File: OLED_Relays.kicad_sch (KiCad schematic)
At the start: 0 parts

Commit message: OLED, Relay and Bar graph added
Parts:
- added BAR1: HDSP-4830_2, Display:HDSP-4830, symbol LED:HDSP-4830_2
- added D17, D18: 1N4148, Diode_THT:D_DO-35_SOD27_P7.62mm_Horizontal, symbol Lattice_DVK:1N4148
- added J3, J4: Relay, TerminalBlock_Phoenix:TerminalBlock_Phoenix_MKDS-1,5-3-5.08_1x03_P5.08mm_Horizontal, symbol Lattice_DVK:Screw_Terminal_01x03
- added J5: RELAY, symbol Connector:Conn_01x04_Pin
- added J6: OLED, symbol Connector:Conn_01x04_Pin
- added K1: SANYOU_SRD_Form_C, LOGSUN:LGS-KC-FRS1B, symbol Lattice_DVK:SANYOU_SRD_Form_C_1
- added K2: SANYOU_SRD_Form_C, LOGSUN:LGS-KC-FRS1B, symbol Lattice_DVK:SANYOU_SRD_Form_C
- added Q4, Q5: BC847, Package_TO_SOT_SMD:SOT-23, symbol Lattice_DVK:BC847
- added Q6, Q7: BC858, Package_TO_SOT_SMD:SOT-23, symbol Lattice_DVK:BC858
- added R28, R29, R32, R33: 4.7K, Resistor_SMD:R_1206_3216Metric_Pad1.30x1.75mm_HandSolder, symbol Lattice_DVK:R_Small
- added R30, R31, R34, R35: 10K, Resistor_SMD:R_1206_3216Metric_Pad1.30x1.75mm_HandSolder, symbol Lattice_DVK:R_Small
- added RN1, RN2, RN3: R_Pack04, symbol Device:R_Pack04
- added SV1: Bar_Graph-I, LOGSUN:LGS-KC-ML10_INTERFACE, symbol LOGSUN:LGS-KC-ML10_INTERFACE
- added SV2: Bar_Graph-II, LOGSUN:LGS-KC-ML10_INTERFACE, symbol LOGSUN:LGS-KC-ML10_INTERFACE
- added U5: 0.96" OLED(I2C), nitin:OLED I2C, symbol NITIN:OLED_I2C
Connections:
- new net: Q4.1 (B), R28.2, R30.1
- new net: Q7.1 (B), R33.1, R35.2
- new net: D18.1 (K), K2.3, Q7.3 (C)
- new net: D17.1 (K), K1.3, Q6.3 (C)
- new net: Q6.1 (B), R32.1, R34.2
- new net: Q4.3 (C), R32.2
- new net: Q5.3 (C), R33.2
- new net: Q5.1 (B), R29.2, R31.1
- new net BAR 1: BAR1.1 (A), RN1.8 (R1.2)
- new net BAR 10: BAR1.10 (A), RN3.7 (R2.2)
- new net BAR 2: BAR1.2 (A), RN1.7 (R2.2)
- new net BAR 3: BAR1.3 (A), RN1.6 (R3.2)
- new net BAR 4: BAR1.4 (A), RN1.5 (R4.2)
- new net BAR 5: BAR1.5 (A), RN2.8 (R1.2)
- new net BAR 6: BAR1.6 (A), RN2.7 (R2.2)
- new net BAR 7: BAR1.7 (A), RN2.6 (R3.2)
- new net BAR 8: BAR1.8 (A), RN2.5 (R4.2)
- new net BAR 9: BAR1.9 (A), RN3.8 (R1.2)
- new net COM_1: J3.2 (Pin_2), K1.5, K1.6
- new net COM_2: J4.2 (Pin_2), K2.5, K2.6
- new net GND_{Bar}: BAR1.11 (K), BAR1.12 (K), BAR1.13 (K), BAR1.14 (K), BAR1.15 (K), BAR1.16 (K), BAR1.17 (K), BAR1.18 (K), BAR1.19 (K), BAR1.20 (K), SV1.2, SV2.2
- new net GND_{OLED}: J6.4 (Pin_4), U5.2 (GND)
- new net GND_{RB}: D17.2 (A), D18.2 (A), J5.4 (Pin_4), K1.4, K2.4, Q4.2 (E), Q5.2 (E), R30.2, R31.2
- new net LD 1: SV1.3
- new net LD 2: SV1.4
- new net LD 3: SV1.5
- new net LD 4: SV1.6
- new net LD 5: SV1.7
- new net LD 6: SV1.8
- new net LD 7: SV1.9
- new net LD 8: SV1.10
- new net NC_1: J3.3 (Pin_3), K1.2
- new net NC_2: J4.3 (Pin_3), K2.2
- new net NO_1: J3.1 (Pin_1), K1.1
- new net NO_2: J4.1 (Pin_1), K2.1
- new net Relay_1: J5.2 (Pin_2), R28.1
- new net Relay_2: J5.3 (Pin_3), R29.1
- new net SCL: J6.2 (Pin_2), U5.3 (SCL)
- new net SDA: J6.3 (Pin_3), U5.4 (SDA)
- new net VCC_{OLED}: J6.1 (Pin_1), U5.1 (VCC)
- new net VCC_{RB}: J5.1 (Pin_1), Q6.2 (E), Q7.2 (E), R34.1, R35.1
- no-connect marks 0 -> 12
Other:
- note added: "0.96" OLED"
- note added: "Connectors"
- note added: "LED-Bar-Graph"
- note added: "Relay_{1}"
- note added: "Relay_{2}"

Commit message: Schematic Completed, Footprints Assigned
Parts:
- J3: value Relay -> Relay_1
- J4: value Relay -> Relay_2
- J5, J6: footprint (none) -> Connector_JST:JST_EH_B4B-EH-A_1x04_P2.50mm_Vertical
- R28, R29, R30, R31, R32, R33, R34, R35: footprint Resistor_SMD:R_1206_3216Metric_Pad1.30x1.75mm_HandSolder -> Resistor_SMD:R_0805_2012Metric_Pad1.20x1.40mm_HandSolder
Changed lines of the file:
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@@
 			)
 		)
-		(property "Footprint" "Resistor_SMD:R_1206_3216Metric_Pad1.30x1.75mm_HandSolder"
+		(property "Footprint" "Resistor_SMD:R_0805_2012Metric_Pad1.20x1.40mm_HandSolder"
 			(at 39.37 45.72 0)
 			(effects
@@
 			)
 		)
-		(property "Value" "Relay"
+		(property "Value" "Relay_1"
 			(at 132.08 49.5299 0)
 			(effects
@@
 			)
 		)
-		(property "Footprint" ""
+		(property "Footprint" "Connector_JST:JST_EH_B4B-EH-A_1x04_P2.50mm_Vertical"
 			(at 34.544 167.894 0)
 			(effects
@@
 			)
 		)
-		(property "Footprint" ""
+		(property "Footprint" "Connector_JST:JST_EH_B4B-EH-A_1x04_P2.50mm_Vertical"
 			(at 71.12 167.64 0)
 			(effects
@@
 			)
 		)
-		(property "Footprint" "Resistor_SMD:R_1206_3216Metric_Pad1.30x1.75mm_HandSolder"
+		(property "Footprint" "Resistor_SMD:R_0805_2012Metric_Pad1.20x1.40mm_HandSolder"
 			(at 74.93 29.21 0)
 			(effects
@@
 			)
 		)
-		(property "Footprint" "Resistor_SMD:R_1206_3216Metric_Pad1.30x1.75mm_HandSolder"
+		(property "Footprint" "Resistor_SMD:R_0805_2012Metric_Pad1.20x1.40mm_HandSolder"
 			(at 62.23 101.6 0)
 			(effects
@@
 			)
 		)
-		(property "Footprint" "Resistor_SMD:R_1206_3216Metric_Pad1.30x1.75mm_HandSolder"
+		(property "Footprint" "Resistor_SMD:R_0805_2012Metric_Pad1.20x1.40mm_HandSolder"
 			(at 74.93 97.79 0)
 			(effects
@@
 			)
 		)
-		(property "Footprint" "Resistor_SMD:R_1206_3216Metric_Pad1.30x1.75mm_HandSolder"
+		(property "Footprint" "Resistor_SMD:R_0805_2012Metric_Pad1.20x1.40mm_HandSolder"
 			(at 39.37 114.3 0)
 			(effects
@@
 			)
 		)
-		(property "Footprint" "Resistor_SMD:R_1206_3216Metric_Pad1.30x1.75mm_HandSolder"
+		(property "Footprint" "Resistor_SMD:R_0805_2012Metric_Pad1.20x1.40mm_HandSolder"
 			(at 48.26 120.65 0)
 			(effects
@@
 			)
 		)
-		(property "Value" "Relay"
+		(property "Value" "Relay_2"
 			(at 132.08 118.1099 0)
 			(effects
@@
 			)
 		)
-		(property "Footprint" "Resistor_SMD:R_1206_3216Metric_Pad1.30x1.75mm_HandSolder"
+		(property "Footprint" "Resistor_SMD:R_0805_2012Metric_Pad1.20x1.40mm_HandSolder"
 			(at 62.23 33.02 0)
 			(effects
@@
 			)
 		)
-		(property "Footprint" "Resistor_SMD:R_1206_3216Metric_Pad1.30x1.75mm_HandSolder"
+		(property "Footprint" "Resistor_SMD:R_0805_2012Metric_Pad1.20x1.40mm_HandSolder"
 			(at 48.26 52.07 0)
 			(effects

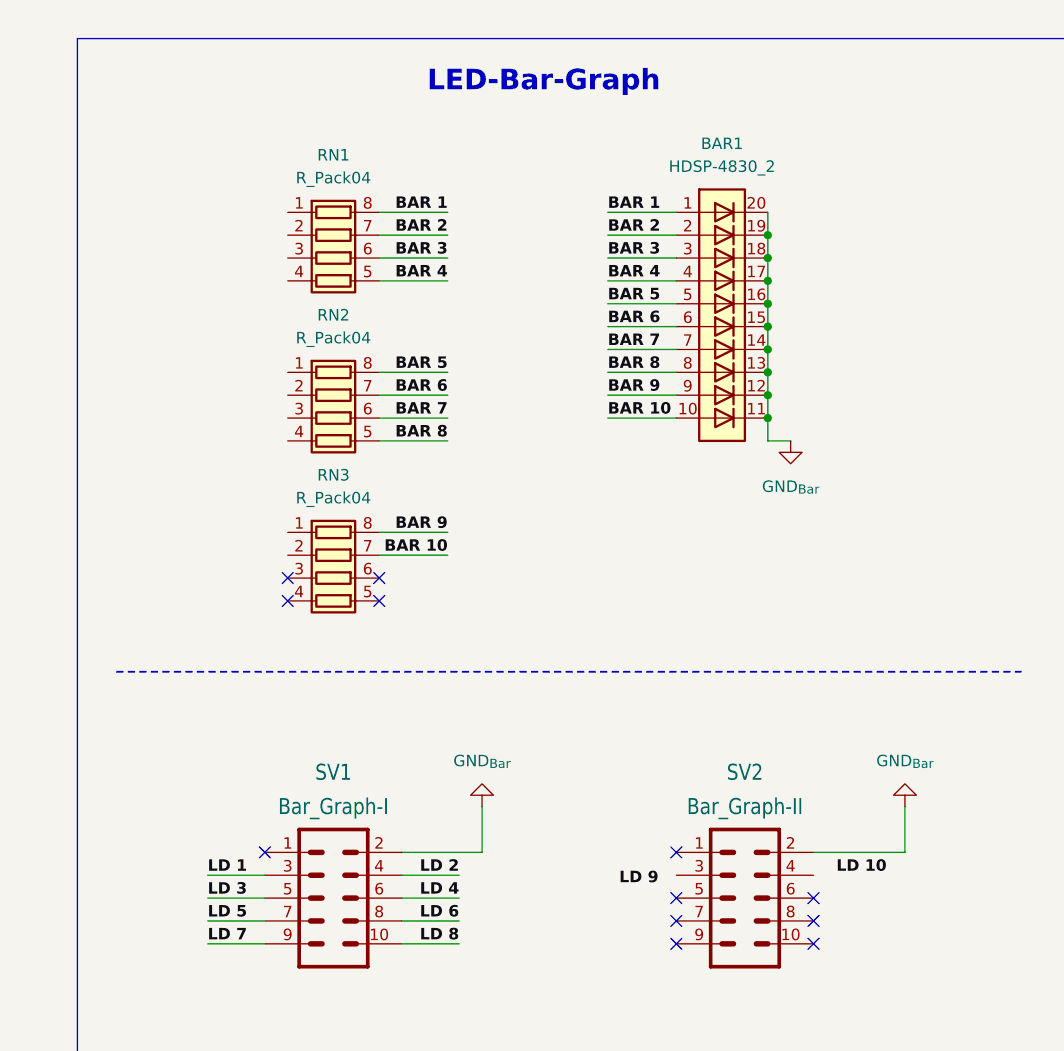
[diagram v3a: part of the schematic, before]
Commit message: Bar LED Resistors Added & Mounting holes added
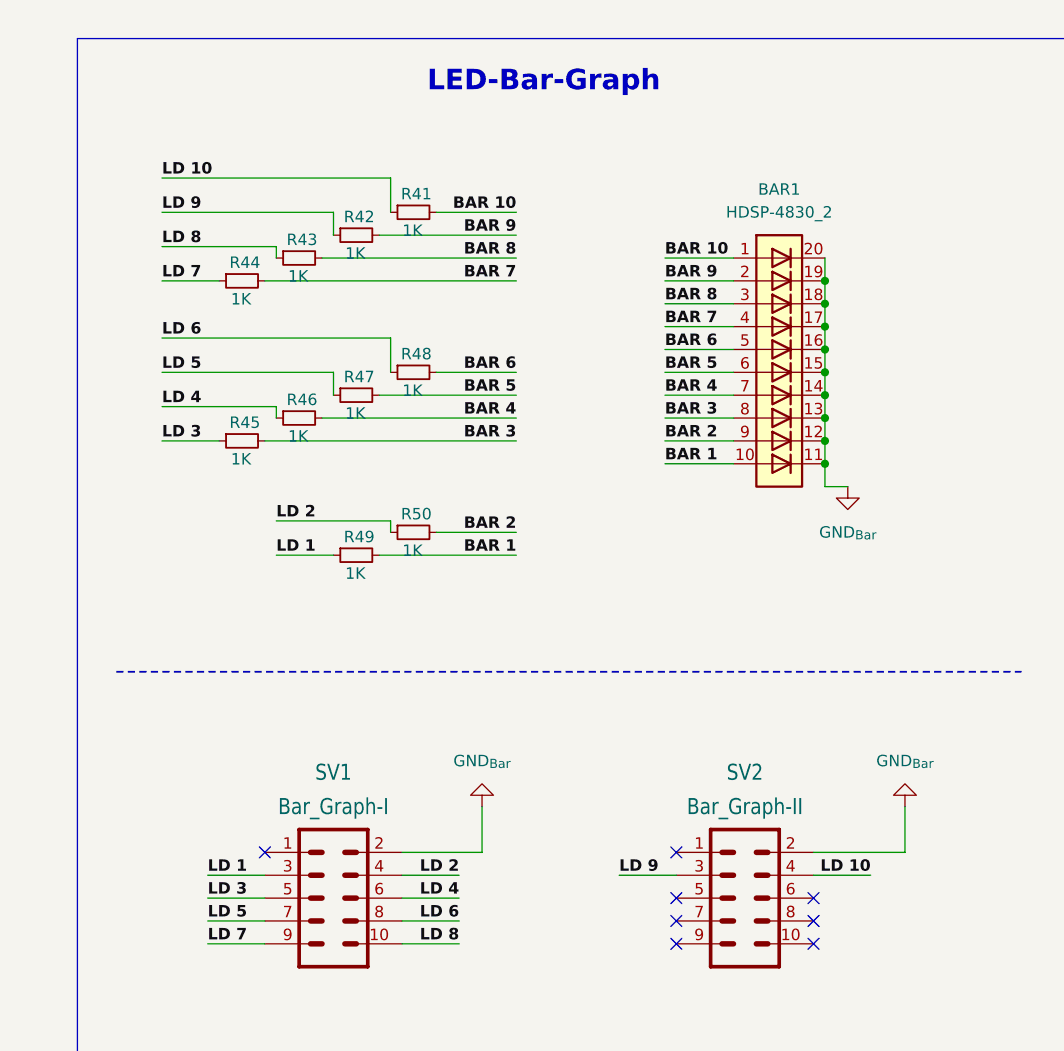
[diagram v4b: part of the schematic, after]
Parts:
- removed RN1, RN2, RN3: R_Pack04, symbol Device:R_Pack04
- added R41, R42, R43, R44, R45, R46, R47, R48, R49, R50: 1K, Resistor_SMD:R_0805_2012Metric_Pad1.20x1.40mm_HandSolder, symbol Lattice_DVK:R_Small
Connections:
- net BAR 1: now also BAR1.10 (A), R49.2; no longer BAR1.1 (A)
- net BAR 10: now also BAR1.1 (A), R41.2; no longer BAR1.10 (A)
- net BAR 2: now also BAR1.9 (A), R50.2; no longer BAR1.2 (A)
- net BAR 3: now also BAR1.8 (A), R45.2; no longer BAR1.3 (A)
- net BAR 4: now also BAR1.7 (A), R46.2; no longer BAR1.4 (A)
- net BAR 5: now also BAR1.6 (A), R47.2; no longer BAR1.5 (A)
- net BAR 6: now also BAR1.5 (A), R48.2; no longer BAR1.6 (A)
- net BAR 7: now also BAR1.4 (A), R44.2; no longer BAR1.7 (A)
- net BAR 8: now also BAR1.3 (A), R43.2; no longer BAR1.8 (A)
- net BAR 9: now also BAR1.2 (A), R42.2; no longer BAR1.9 (A)
- net LD 1: now also R49.1
- net LD 10: now also SV2.4, R41.1
- net LD 2: now also R50.1
- net LD 3: now also R45.1
- net LD 4: now also R46.1
- net LD 5: now also R47.1
- net LD 6: now also R48.1
- net LD 7: now also R44.1
- net LD 8: now also R43.1
- net LD 9: now also SV2.3, R42.1
- no-connect marks 12 -> 8
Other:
- moved on the sheet: BAR1

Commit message: Symbol and footprint library exported
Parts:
- BAR1: symbol LED:HDSP-4830_2 -> ESP32_Xbee_LoRa:HDSP-4830_2
- D17, D18: symbol Lattice_DVK:1N4148 -> ESP32_Xbee_LoRa:1N4148
- J3, J4: symbol Lattice_DVK:Screw_Terminal_01x03 -> ESP32_Xbee_LoRa:Screw_Terminal_01x03
- J5, J6: symbol Connector:Conn_01x04_Pin -> ESP32_Xbee_LoRa:Conn_01x04_Pin
- K1: symbol Lattice_DVK:SANYOU_SRD_Form_C_1 -> ESP32_Xbee_LoRa:SANYOU_SRD_Form_C_1
- K2: symbol Lattice_DVK:SANYOU_SRD_Form_C -> ESP32_Xbee_LoRa:SANYOU_SRD_Form_C
- Q4, Q5: symbol Lattice_DVK:BC847 -> ESP32_Xbee_LoRa:BC847
- Q6, Q7: symbol Lattice_DVK:BC858 -> ESP32_Xbee_LoRa:BC858
- R28, R29, R30, R31, R32, R33, R34, R35, R41, R42, R43, R44, R45, R46, R47, R48, R49, R50: symbol Lattice_DVK:R_Small -> ESP32_Xbee_LoRa:R_Small
- SV1, SV2: symbol LOGSUN:LGS-KC-ML10_INTERFACE -> ESP32_Xbee_LoRa:LGS-KC-ML10_INTERFACE
- U5: symbol NITIN:OLED_I2C -> ESP32_Xbee_LoRa:OLED_I2C
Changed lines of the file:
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@@
 	)
 	(symbol
-		(lib_id "power:VCC")
+		(lib_id "ESP32_Xbee_LoRa:VCC")
 		(at 116.84 168.91 0)
 		(unit 1)
@@
 	)
 	(symbol
-		(lib_id "NITIN:OLED_I2C")
+		(lib_id "ESP32_Xbee_LoRa:OLED_I2C")
 		(at 124.46 173.99 0)
 		(unit 1)
@@
 	)
 	(symbol
-		(lib_id "power:GND")
+		(lib_id "ESP32_Xbee_LoRa:GND")
 		(at 252.73 101.6 180)
 		(unit 1)
@@
 	)
 	(symbol
-		(lib_id "power:VCC")
+		(lib_id "ESP32_Xbee_LoRa:VCC")
 		(at 77.47 179.07 270)
 		(unit 1)
@@
 	)
 	(symbol
-		(lib_id "power:VCC")
+		(lib_id "ESP32_Xbee_LoRa:VCC")
 		(at 38.354 174.244 270)
 		(unit 1)
@@
 	)
 	(symbol
-		(lib_id "Lattice_DVK:R_Small")
+		(lib_id "ESP32_Xbee_LoRa:R_Small")
 		(at 39.37 45.72 90)
 		(unit 1)
@@
 	)
 	(symbol
-		(lib_id "Lattice_DVK:R_Small")
+		(lib_id "ESP32_Xbee_LoRa:R_Small")
 		(at 198.12 71.12 90)
 		(mirror x)
@@
 	)
 	(symbol
-		(lib_id "Lattice_DVK:Screw_Terminal_01x03")
+		(lib_id "ESP32_Xbee_LoRa:Screw_Terminal_01x03")
 		(at 129.54 48.26 0)
 		(unit 1)
@@
 	)
 	(symbol
-		(lib_id "power:GND")
+		(lib_id "ESP32_Xbee_LoRa:GND")
 		(at 86.36 134.62 0)
 		(unit 1)
@@
 	)
 	(symbol
-		(lib_id "Lattice_DVK:R_Small")
+		(lib_id "ESP32_Xbee_LoRa:R_Small")
 		(at 179.07 43.18 90)
 		(mirror x)
@@
 	)
 	(symbol
-		(lib_id "power:GND")
+		(lib_id "ESP32_Xbee_LoRa:GND")
 		(at 86.36 66.04 0)
 		(unit 1)
@@
 	)
 	(symbol
-		(lib_id "power:GND")
+		(lib_id "ESP32_Xbee_LoRa:GND")
 		(at 63.5 177.8 270)
 		(unit 1)
@@
 	)
 	(symbol
-		(lib_id "Lattice_DVK:BC858")
+		(lib_id "ESP32_Xbee_LoRa:BC858")
 		(at 83.82 101.6 0)
 		(mirror x)
@@
 	)
 	(symbol
-		(lib_id "Connector:Conn_01x04_Pin")
+		(lib_id "ESP32_Xbee_LoRa:Conn_01x04_Pin")
 		(at 34.544 167.894 270)
 		(unit 1)
@@
 	)
 	(symbol
-		(lib_id "LOGSUN:LGS-KC-ML10_INTERFACE")
+		(lib_id "ESP32_Xbee_LoRa:LGS-KC-ML10_INTERFACE")
 		(at 189.23 111.76 180)
 		(unit 1)
@@
 	)
 	(symbol
-		(lib_id "Connector:Conn_01x04_Pin")
+		(lib_id "ESP32_Xbee_LoRa:Conn_01x04_Pin")
 		(at 71.12 167.64 270)
 		(unit 1)
@@
 	)
 	(symbol
-		(lib_id "power:GND")
+		(lib_id "ESP32_Xbee_LoRa:GND")
 		(at 205.74 101.6 180)
 		(unit 1)
@@
 	(symbol
 		(lib_name "SANYOU_SRD_Form_C_1")
-		(lib_id "Lattice_DVK:SANYOU_SRD_Form_C_1")
+		(lib_id "ESP32_Xbee_LoRa:SANYOU_SRD_Form_C_1")
 		(at 91.44 52.07 0)
 		(unit 1)
@@
 	)
 	(symbol
-		(lib_id "Lattice_DVK:R_Small")
+		(lib_id "ESP32_Xbee_LoRa:R_Small")
 		(at 198.12 35.56 90)
 		(mirror x)
@@
 	)
 	(symbol
-		(lib_id "Lattice_DVK:R_Small")
+		(lib_id "ESP32_Xbee_LoRa:R_Small")
 		(at 191.77 38.1 90)
 		(mirror x)
@@
 	)
 	(symbol
-		(lib_id "Lattice_DVK:R_Small")
+		(lib_id "ESP32_Xbee_LoRa:R_Small")
 		(at 185.42 40.64 90)
 		(mirror x)
@@
 	)
 	(symbol
-		(lib_id "LOGSUN:LGS-KC-ML10_INTERFACE")
+		(lib_id "ESP32_Xbee_LoRa:LGS-KC-ML10_INTERFACE")
 		(at 234.95 111.76 180)
 		(unit 1)
@@
 	)
 	(symbol
-		(lib_id "Lattice_DVK:R_Small")
+		(lib_id "ESP32_Xbee_LoRa:R_Small")
 		(at 179.07 60.96 90)
 		(mirror x)
@@
 	)
 	(symbol
-		(lib_id "Lattice_DVK:R_Small")
+		(lib_id "ESP32_Xbee_LoRa:R_Small")
 		(at 185.42 58.42 90)
 		(mirror x)
@@
 	)
 	(symbol
-		(lib_id "Lattice_DVK:1N4148")
+		(lib_id "ESP32_Xbee_LoRa:1N4148")
 		(at 74.93 120.65 90)
 		(unit 1)
@@
 	)
 	(symbol
-		(lib_id "Lattice_DVK:R_Small")
+		(lib_id "ESP32_Xbee_LoRa:R_Small")
 		(at 74.93 29.21 0)
 		(mirror y)
@@
 	)
 	(symbol
-		(lib_id "Lattice_DVK:BC847")
+		(lib_id "ESP32_Xbee_LoRa:BC847")
 		(at 55.88 45.72 0)
 		(unit 1)
@@
 	)
 	(symbol
-		(lib_id "Lattice_DVK:SANYOU_SRD_Form_C")
+		(lib_id "ESP32_Xbee_LoRa:SANYOU_SRD_Form_C")
 		(at 91.44 120.65 0)
 		(unit 1)
@@
 	)
 	(symbol
-		(lib_id "power:GND")
+		(lib_id "ESP32_Xbee_LoRa:GND")
 		(at 246.38 66.04 0)
 		(unit 1)
@@
 	)
 	(symbol
-		(lib_id "Lattice_DVK:R_Small")
+		(lib_id "ESP32_Xbee_LoRa:R_Small")
 		(at 62.23 101.6 270)
 		(mirror x)
@@
 	)
 	(symbol
-		(lib_id "power:VCC")
+		(lib_id "ESP32_Xbee_LoRa:VCC")
 		(at 86.36 22.86 0)
 		(unit 1)
@@
 	)
 	(symbol
-		(lib_id "Lattice_DVK:R_Small")
+		(lib_id "ESP32_Xbee_LoRa:R_Small")
 		(at 191.77 55.88 90)
 		(mirror x)
@@
 	)
 	(symbol
-		(lib_id "Lattice_DVK:BC847")
+		(lib_id "ESP32_Xbee_LoRa:BC847")
 		(at 55.88 114.3 0)
 		(unit 1)
@@
 	)
 	(symbol
-		(lib_id "Lattice_DVK:R_Small")
+		(lib_id "ESP32_Xbee_LoRa:R_Small")
 		(at 74.93 97.79 0)
 		(mirror y)
@@
 	)
 	(symbol
-		(lib_id "Lattice_DVK:R_Small")
+		(lib_id "ESP32_Xbee_LoRa:R_Small")
 		(at 39.37 114.3 90)
 		(unit 1)
@@
 	)
 	(symbol
-		(lib_id "Logsun_Logo:LOGO")
+		(lib_id "ESP32_Xbee_LoRa:LOGO")
 		(at 260.35 172.72 0)
 		(unit 1)
@@
 	)
 	(symbol
-		(lib_id "power:VCC")
+		(lib_id "ESP32_Xbee_LoRa:VCC")
 		(at 86.36 91.44 0)
 		(unit 1)
@@
 	)
 	(symbol
-		(lib_id "Lattice_DVK:R_Small")
+		(lib_id "ESP32_Xbee_LoRa:R_Small")
 		(at 191.77 73.66 90)
 		(mirror x)
@@
 	)
 	(symbol
-		(lib_id "Lattice_DVK:R_Small")
+		(lib_id "ESP32_Xbee_LoRa:R_Small")
 		(at 48.26 120.65 0)
 		(unit 1)
@@
 	)
 	(symbol
-		(lib_id "Lattice_DVK:Screw_Terminal_01x03")
+		(lib_id "ESP32_Xbee_LoRa:Screw_Terminal_01x03")
 		(at 129.54 116.84 0)
 		(unit 1)
@@
 	)
 	(symbol
-		(lib_id "Lattice_DVK:R_Small")
+		(lib_id "ESP32_Xbee_LoRa:R_Small")
 		(at 62.23 33.02 270)
 		(mirror x)
@@
 	)
 	(symbol
-		(lib_id "power:GND")
+		(lib_id "ESP32_Xbee_LoRa:GND")
 		(at 28.194 174.244 270)
 		(unit 1)
@@
 	)
 	(symbol
-		(lib_id "Lattice_DVK:1N4148")
+		(lib_id "ESP32_Xbee_LoRa:1N4148")
 		(at 74.93 52.07 90)
 		(unit 1)
@@
 	)
 	(symbol
-		(lib_id "Lattice_DVK:R_Small")
+		(lib_id "ESP32_Xbee_LoRa:R_Small")
 		(at 198.12 53.34 90)
 		(mirror x)
@@
 	)
 	(symbol
-		(lib_id "LED:HDSP-4830_2")
+		(lib_id "ESP32_Xbee_LoRa:HDSP-4830_2")
 		(at 238.76 50.8 0)
 		(unit 1)
@@
 	)
 	(symbol
-		(lib_id "power:GND")
+		(lib_id "ESP32_Xbee_LoRa:GND")
 		(at 111.76 173.99 270)
 		(unit 1)
@@
 	)
 	(symbol
-		(lib_id "Lattice_DVK:BC858")
+		(lib_id "ESP32_Xbee_LoRa:BC858")
 		(at 83.82 33.02 0)
 		(mirror x)
@@
 	)
 	(symbol
-		(lib_id "Lattice_DVK:R_Small")
+		(lib_id "ESP32_Xbee_LoRa:R_Small")
 		(at 48.26 52.07 0)
 		(unit 1)
